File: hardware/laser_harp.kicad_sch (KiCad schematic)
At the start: 4 parts, among them U1 DAC_XY, U2 DAC_RG, U3 DAC_BI, U4 ESP32-S3

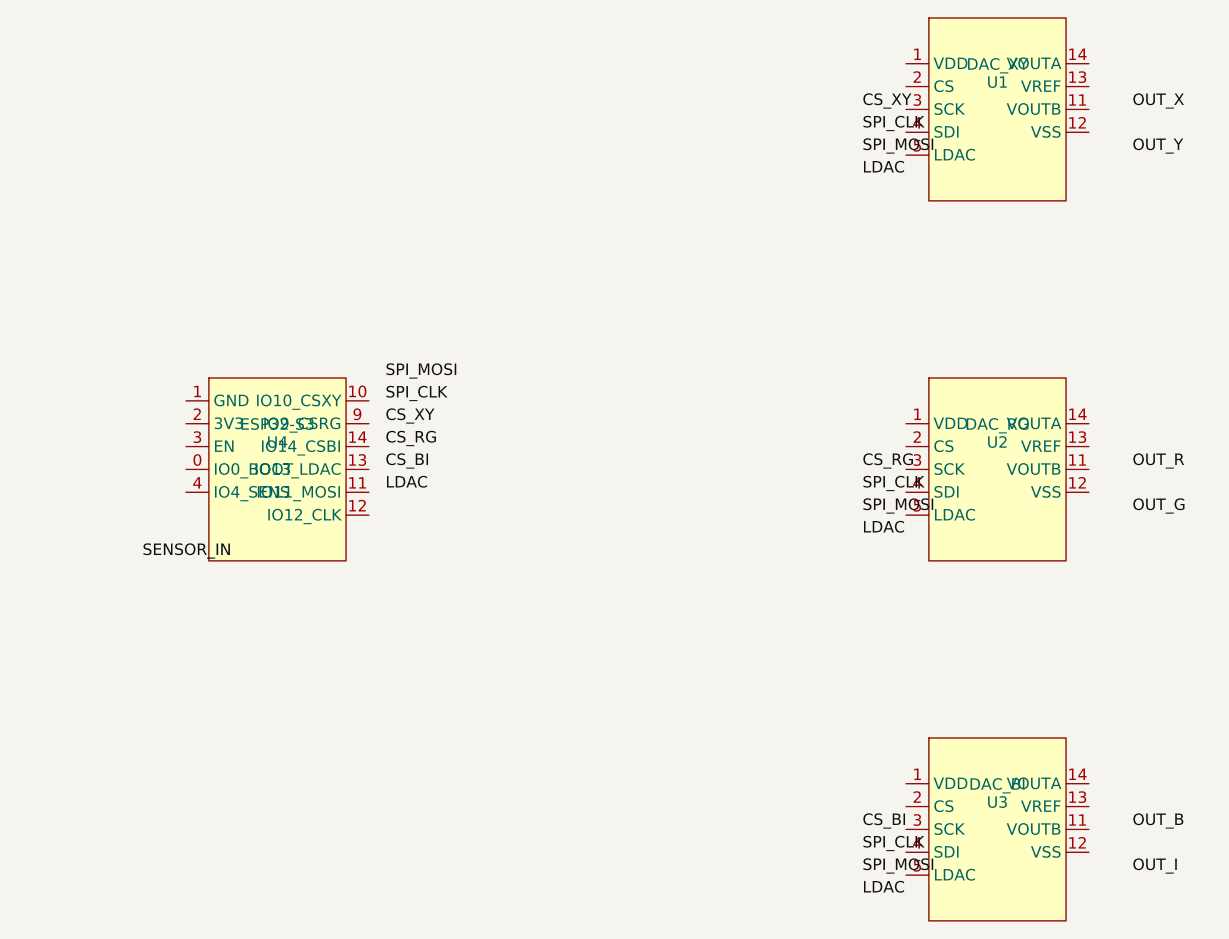
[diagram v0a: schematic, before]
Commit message: Fix KiCad schematic coordinates and refactor generation script
- Corrected coordinate system assumption (KiCad uses Y-down).
- Updated symbol generation to order pins Top-to-Bottom.
- Refactored `KiCadSchematicGenerator` to use `symbol_pin_map` and `instance_map` for robust pin lookups.
- Replaced magic number coordinate calculations with `connect_pin` helper using stored metadata.
- Ensured labels and wire stubs are correctly placed relative to pins.

Co-authored-by: Leonrts <258967714+Leonrts@users.noreply.github.com>
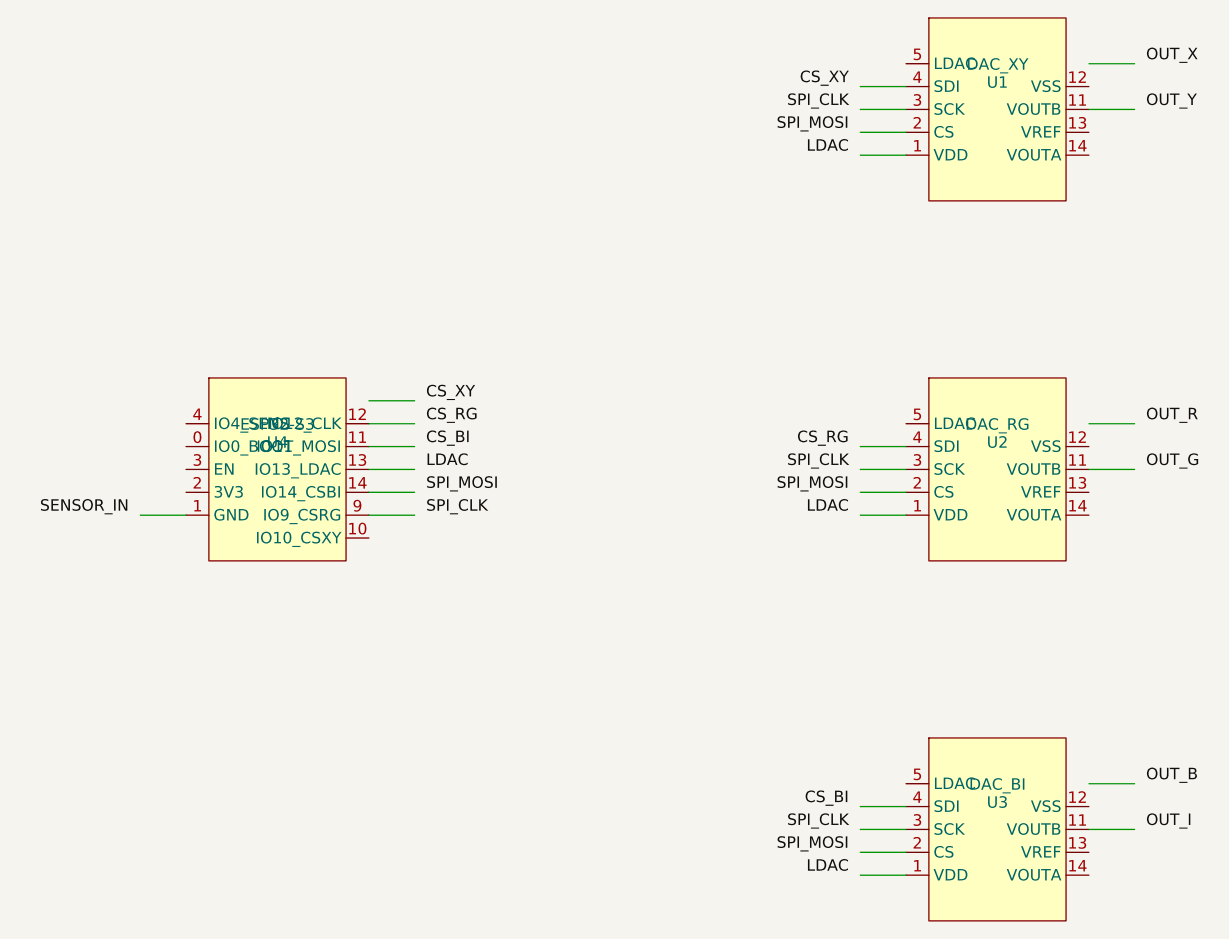
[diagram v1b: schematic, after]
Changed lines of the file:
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@@
     )
   )
-  (label "SPI_MOSI" (at 112 90 0) (fields_autoplaced)
+  (wire (pts (xy 89.84 105.08) (xy 84.76 105.08))
+    (stroke (width 0) (type default) (color 0 0 0 0))
+  )
+  (wire (pts (xy 110.16 92.38) (xy 115.24 92.38))
+    (stroke (width 0) (type default) (color 0 0 0 0))
+  )
+  (wire (pts (xy 110.16 94.92) (xy 115.24 94.92))
+    (stroke (width 0) (type default) (color 0 0 0 0))
+  )
+  (wire (pts (xy 110.16 97.46) (xy 115.24 97.46))
+    (stroke (width 0) (type default) (color 0 0 0 0))
+  )
+  (wire (pts (xy 110.16 100.0) (xy 115.24 100.0))
+    (stroke (width 0) (type default) (color 0 0 0 0))
+  )
+  (wire (pts (xy 110.16 102.54) (xy 115.24 102.54))
+    (stroke (width 0) (type default) (color 0 0 0 0))
+  )
+  (wire (pts (xy 110.16 105.08) (xy 115.24 105.08))
+    (stroke (width 0) (type default) (color 0 0 0 0))
+  )
+  (wire (pts (xy 169.84 57.46) (xy 164.76 57.46))
+    (stroke (width 0) (type default) (color 0 0 0 0))
+  )
+  (wire (pts (xy 169.84 60.0) (xy 164.76 60.0))
+    (stroke (width 0) (type default) (color 0 0 0 0))
+  )
+  (wire (pts (xy 169.84 62.54) (xy 164.76 62.54))
+    (stroke (width 0) (type default) (color 0 0 0 0))
+  )
+  (wire (pts (xy 169.84 65.08) (xy 164.76 65.08))
+    (stroke (width 0) (type default) (color 0 0 0 0))
+  )
+  (wire (pts (xy 190.16 54.92) (xy 195.24 54.92))
+    (stroke (width 0) (type default) (color 0 0 0 0))
+  )
+  (wire (pts (xy 190.16 60.0) (xy 195.24 60.0))
+    (stroke (width 0) (type default) (color 0 0 0 0))
+  )
+  (wire (pts (xy 169.84 97.46) (xy 164.76 97.46))
+    (stroke (width 0) (type default) (color 0 0 0 0))
+  )
+  (wire (pts (xy 169.84 100.0) (xy 164.76 100.0))
+    (stroke (width 0) (type default) (color 0 0 0 0))
+  )
+  (wire (pts (xy 169.84 102.54) (xy 164.76 102.54))
+    (stroke (width 0) (type default) (color 0 0 0 0))
+  )
+  (wire (pts (xy 169.84 105.08) (xy 164.76 105.08))
+    (stroke (width 0) (type default) (color 0 0 0 0))
+  )
+  (wire (pts (xy 190.16 94.92) (xy 195.24 94.92))
+    (stroke (width 0) (type default) (color 0 0 0 0))
+  )
+  (wire (pts (xy 190.16 100.0) (xy 195.24 100.0))
+    (stroke (width 0) (type default) (color 0 0 0 0))
+  )
+  (wire (pts (xy 169.84 137.46) (xy 164.76 137.46))
+    (stroke (width 0) (type default) (color 0 0 0 0))
+  )
+  (wire (pts (xy 169.84 140.0) (xy 164.76 140.0))
+    (stroke (width 0) (type default) (color 0 0 0 0))
+  )
+  (wire (pts (xy 169.84 142.54) (xy 164.76 142.54))
+    (stroke (width 0) (type default) (color 0 0 0 0))
+  )
+  (wire (pts (xy 169.84 145.08) (xy 164.76 145.08))
+    (stroke (width 0) (type default) (color 0 0 0 0))
+  )
+  (wire (pts (xy 190.16 134.92) (xy 195.24 134.92))
+    (stroke (width 0) (type default) (color 0 0 0 0))
+  )
+  (wire (pts (xy 190.16 140.0) (xy 195.24 140.0))
+    (stroke (width 0) (type default) (color 0 0 0 0))
+  )
+  (label "SENSOR_IN" (at 83.49000000000001 105.08 0) (fields_autoplaced)
+    (effects (font (size 1.27 1.27)) (justify right bottom))
+  )
+  (label "CS_XY" (at 116.50999999999999 92.38 0) (fields_autoplaced)
     (effects (font (size 1.27 1.27)) (justify left bottom))
   )
-  (label "SPI_CLK" (at 112 92.5 0) (fields_autoplaced)
+  (label "CS_RG" (at 116.50999999999999 94.92 0) (fields_autoplaced)
     (effects (font (size 1.27 1.27)) (justify left bottom))
   )
-  (label "CS_XY" (at 112 95 0) (fields_autoplaced)
+  (label "CS_BI" (at 116.50999999999999 97.46 0) (fields_autoplaced)
     (effects (font (size 1.27 1.27)) (justify left bottom))
   )
-  (label "CS_RG" (at 112 97.5 0) (fields_autoplaced)
+  (label "LDAC" (at 116.50999999999999 100.0 0) (fields_autoplaced)
     (effects (font (size 1.27 1.27)) (justify left bottom))
   )
-  (label "CS_BI" (at 112 100 0) (fields_autoplaced)
+  (label "SPI_MOSI" (at 116.50999999999999 102.54 0) (fields_autoplaced)
     (effects (font (size 1.27 1.27)) (justify left bottom))
   )
-  (label "LDAC" (at 112 102.5 0) (fields_autoplaced)
+  (label "SPI_CLK" (at 116.50999999999999 105.08 0) (fields_autoplaced)
     (effects (font (size 1.27 1.27)) (justify left bottom))
   )
-  (label "SENSOR_IN" (at 85 110 0) (fields_autoplaced)
+  (label "CS_XY" (at 163.48999999999998 57.46 0) (fields_autoplaced)
+    (effects (font (size 1.27 1.27)) (justify right bottom))
+  )
+  (label "SPI_CLK" (at 163.48999999999998 60.0 0) (fields_autoplaced)
+    (effects (font (size 1.27 1.27)) (justify right bottom))
+  )
+  (label "SPI_MOSI" (at 163.48999999999998 62.54 0) (fields_autoplaced)
+    (effects (font (size 1.27 1.27)) (justify right bottom))
+  )
+  (label "LDAC" (at 163.48999999999998 65.08 0) (fields_autoplaced)
+    (effects (font (size 1.27 1.27)) (justify right bottom))
+  )
+  (label "OUT_X" (at 196.51000000000002 54.92 0) (fields_autoplaced)
     (effects (font (size 1.27 1.27)) (justify left bottom))
   )
-  (label "SPI_MOSI" (at 165 65 0) (fields_autoplaced)
+  (label "OUT_Y" (at 196.51000000000002 60.0 0) (fields_autoplaced)
     (effects (font (size 1.27 1.27)) (justify left bottom))
   )
-  (label "SPI_CLK" (at 165 62.5 0) (fields_autoplaced)
+  (label "CS_RG" (at 163.48999999999998 97.46 0) (fields_autoplaced)
+    (effects (font (size 1.27 1.27)) (justify right bottom))
+  )
+  (label "SPI_CLK" (at 163.48999999999998 100.0 0) (fields_autoplaced)
+    (effects (font (size 1.27 1.27)) (justify right bottom))
+  )
+  (label "SPI_MOSI" (at 163.48999999999998 102.54 0) (fields_autoplaced)
+    (effects (font (size 1.27 1.27)) (justify right bottom))
+  )
+  (label "LDAC" (at 163.48999999999998 105.08 0) (fields_autoplaced)
+    (effects (font (size 1.27 1.27)) (justify right bottom))
+  )
+  (label "OUT_R" (at 196.51000000000002 94.92 0) (fields_autoplaced)
     (effects (font (size 1.27 1.27)) (justify left bottom))
   )
-  (label "CS_XY" (at 165 60 0) (fields_autoplaced)
+  (label "OUT_G" (at 196.51000000000002 100.0 0) (fields_autoplaced)
     (effects (font (size 1.27 1.27)) (justify left bottom))
   )
-  (label "LDAC" (at 165 67.5 0) (fields_autoplaced)
+  (label "CS_BI" (at 163.48999999999998 137.46 0) (fields_autoplaced)
+    (effects (font (size 1.27 1.27)) (justify right bottom))
+  )
+  (label "SPI_CLK" (at 163.48999999999998 140.0 0) (fields_autoplaced)
+    (effects (font (size 1.27 1.27)) (justify right bottom))
+  )
+  (label "SPI_MOSI" (at 163.48999999999998 142.54 0) (fields_autoplaced)
+    (effects (font (size 1.27 1.27)) (justify right bottom))
+  )
+  (label "LDAC" (at 163.48999999999998 145.08 0) (fields_autoplaced)
+    (effects (font (size 1.27 1.27)) (justify right bottom))
+  )
+  (label "OUT_B" (at 196.51000000000002 134.92 0) (fields_autoplaced)
     (effects (font (size 1.27 1.27)) (justify left bottom))
   )
-  (label "OUT_X" (at 195 60 0) (fields_autoplaced)
-    (effects (font (size 1.27 1.27)) (justify left bottom))
-  )
-  (label "OUT_Y" (at 195 65 0) (fields_autoplaced)
-    (effects (font (size 1.27 1.27)) (justify left bottom))
-  )
-  (label "SPI_MOSI" (at 165 105 0) (fields_autoplaced)
-    (effects (font (size 1.27 1.27)) (justify left bottom))
-  )
-  (label "SPI_CLK" (at 165 102.5 0) (fields_autoplaced)
-    (effects (font (size 1.27 1.27)) (justify left bottom))
-  )
-  (label "CS_RG" (at 165 100 0) (fields_autoplaced)
-    (effects (font (size 1.27 1.27)) (justify left bottom))
-  )
-  (label "LDAC" (at 165 107.5 0) (fields_autoplaced)
-    (effects (font (size 1.27 1.27)) (justify left bottom))
-  )
-  (label "OUT_R" (at 195 100 0) (fields_autoplaced)
-    (effects (font (size 1.27 1.27)) (justify left bottom))
-  )
-  (label "OUT_G" (at 195 105 0) (fields_autoplaced)
-    (effects (font (size 1.27 1.27)) (justify left bottom))
-  )
-  (label "SPI_MOSI" (at 165 145 0) (fields_autoplaced)
-    (effects (font (size 1.27 1.27)) (justify left bottom))
-  )
-  (label "SPI_CLK" (at 165 142.5 0) (fields_autoplaced)
-    (effects (font (size 1.27 1.27)) (justify left bottom))
-  )
-  (label "CS_BI" (at 165 140 0) (fields_autoplaced)
-    (effects (font (size 1.27 1.27)) (justify left bottom))
-  )
-  (label "LDAC" (at 165 147.5 0) (fields_autoplaced)
-    (effects (font (size 1.27 1.27)) (justify left bottom))
-  )
-  (label "OUT_B" (at 195 140 0) (fields_autoplaced)
-    (effects (font (size 1.27 1.27)) (justify left bottom))
-  )
-  (label "OUT_I" (at 195 145 0) (fields_autoplaced)
+  (label "OUT_I" (at 196.51000000000002 140.0 0) (fields_autoplaced)
     (effects (font (size 1.27 1.27)) (justify left bottom))
   ))
